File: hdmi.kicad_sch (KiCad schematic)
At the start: 3 parts

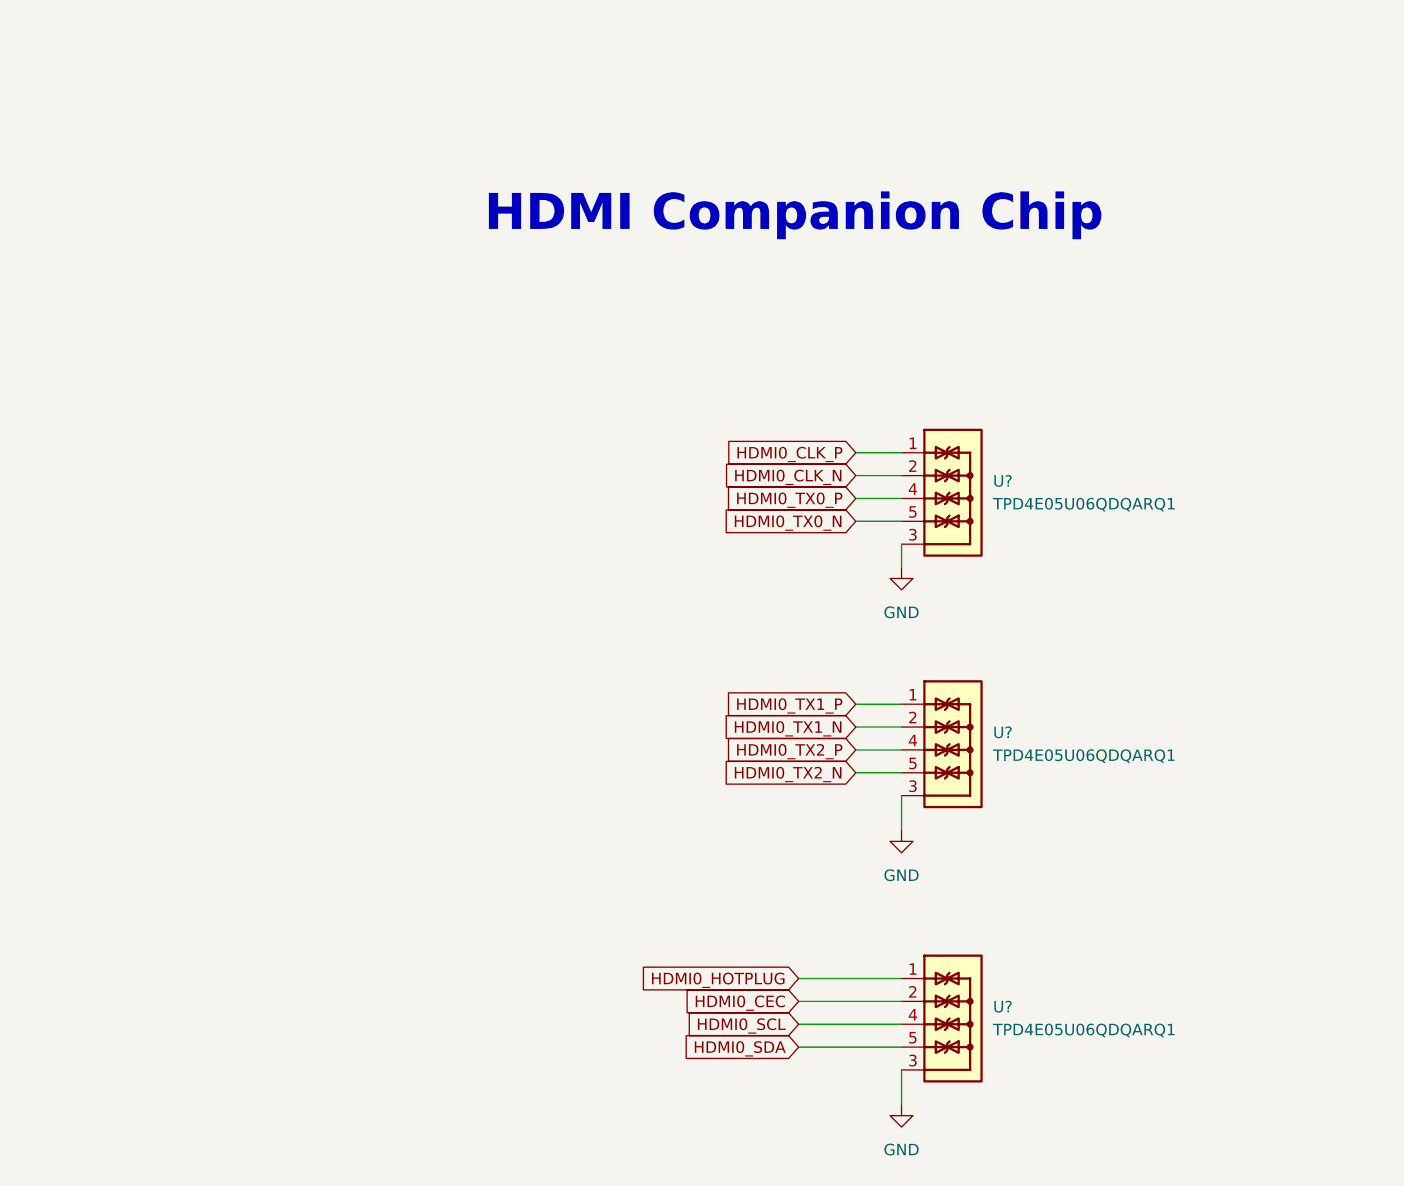
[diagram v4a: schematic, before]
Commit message: [#54016] Place components to assess available space
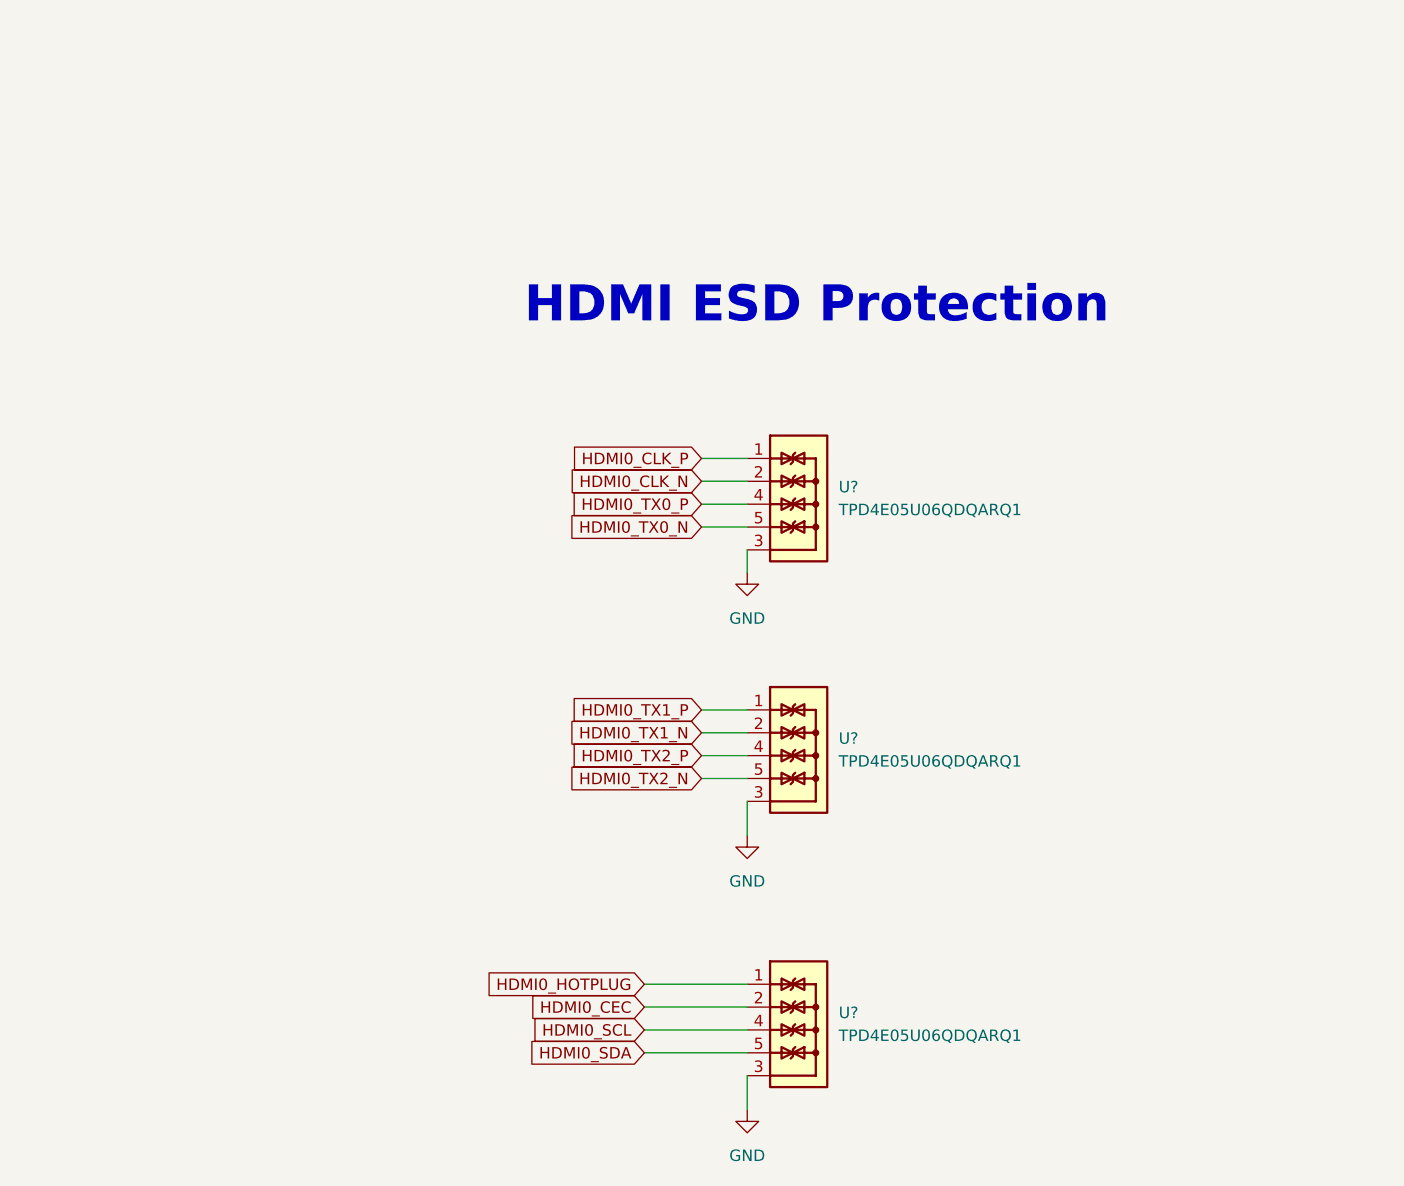
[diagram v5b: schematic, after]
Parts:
- removed U? (x3): TPD4E05U06QDQARQ1, antmicro-footprints:USON-10_2.5x1mm_P0.5mm, symbol antmicroTVSDiodes:TPD4E05U06QDQARQ1
- added U? (x3): TPD4E05U06QDQARQ1, antmicro-footprints:USON-10_2.5x1mm_P0.5mm, symbol antmicroTVSDiodes:TPD4E05U06QDQARQ1
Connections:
- net GND: now also U?.3, U?.3, U?.3, U?.8, U?.8, U?.8
- net HDMI0_CEC: now also U?.2, U?.9
- net HDMI0_CLK_N: now also U?.2, U?.9
- net HDMI0_CLK_P: now also U?.1, U?.10
- net HDMI0_HOTPLUG: now also U?.1, U?.10
- net HDMI0_SCL: now also U?.4, U?.7
- net HDMI0_SDA: now also U?.5, U?.6
- net HDMI0_TX0_N: now also U?.5, U?.6
- net HDMI0_TX0_P: now also U?.4, U?.7
- net HDMI0_TX1_N: now also U?.2, U?.9
- net HDMI0_TX1_P: now also U?.1, U?.10
- net HDMI0_TX2_N: now also U?.5, U?.6
- net HDMI0_TX2_P: now also U?.4, U?.7
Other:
- note added: "HDMI ESD Protection"
- note removed: "HDMI Companion Chip"

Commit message: [#54491] Minor adjustments of labels and graphical items
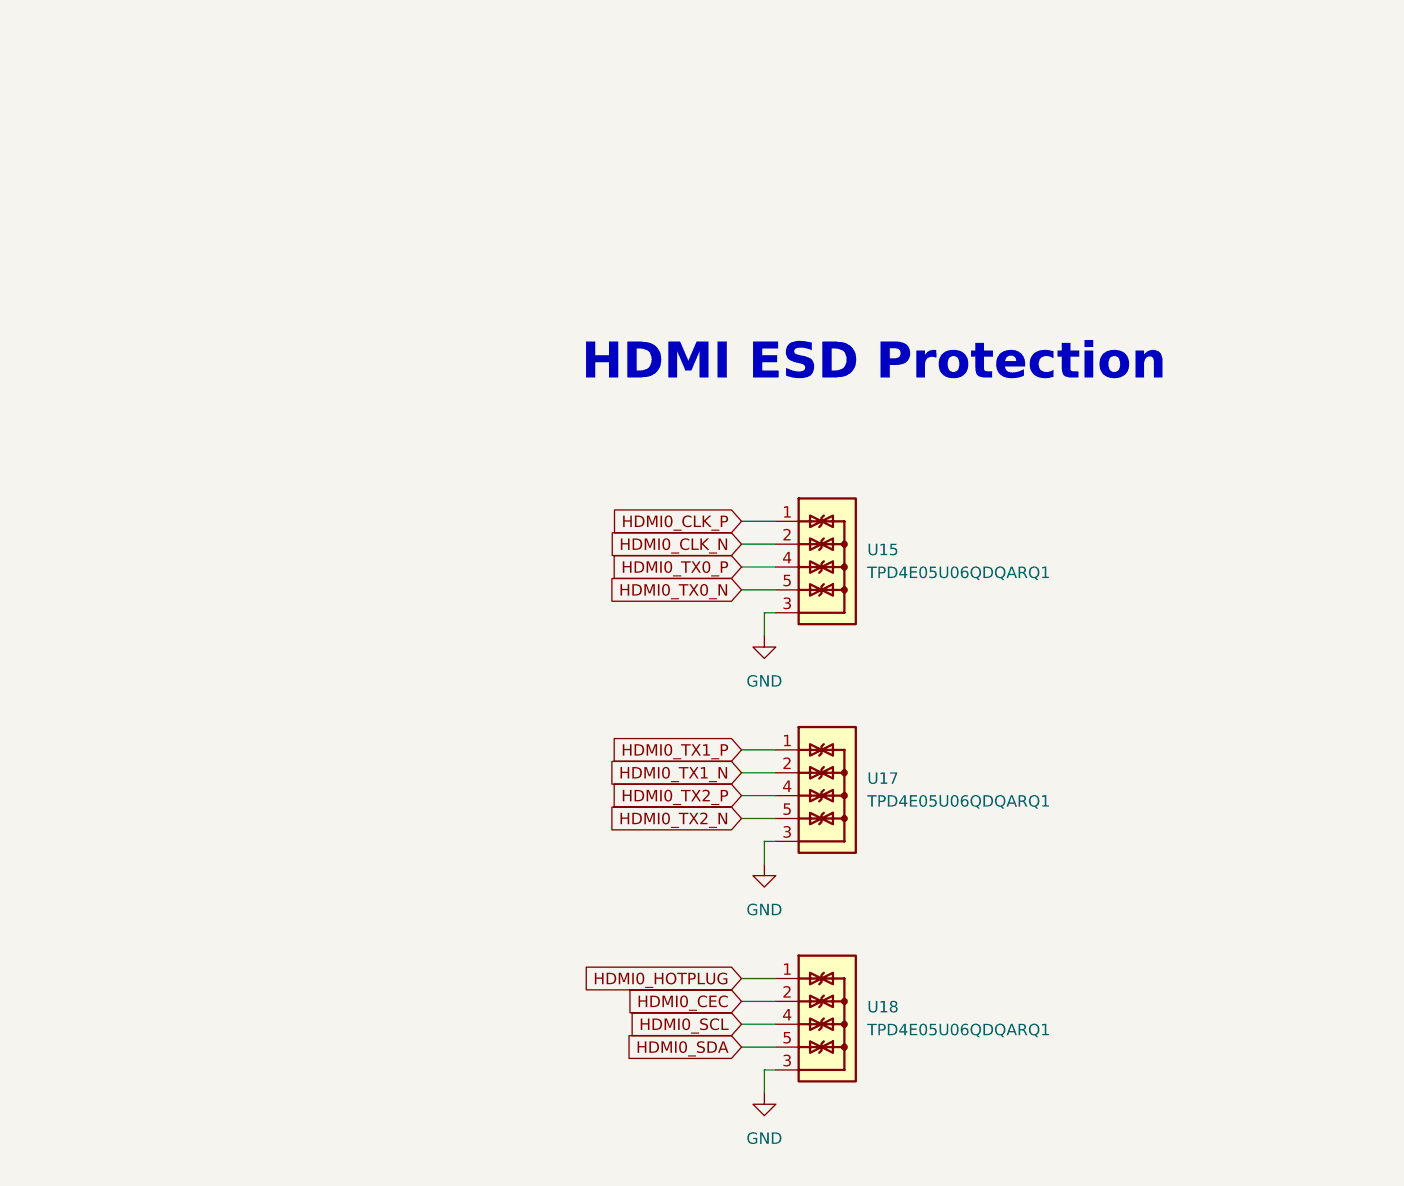
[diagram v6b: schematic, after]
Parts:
- gave numbers to parts that had none: 3
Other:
- moved on the sheet: U15, U17, U18
